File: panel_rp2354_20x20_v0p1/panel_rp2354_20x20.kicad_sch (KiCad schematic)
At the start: 0 parts

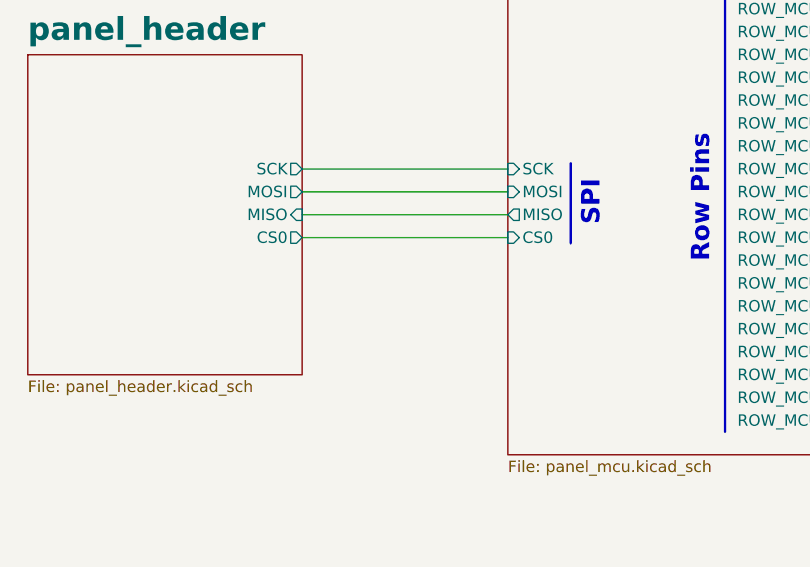
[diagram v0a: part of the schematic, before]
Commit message: Add MISO series resistor and connect EINT to MCU
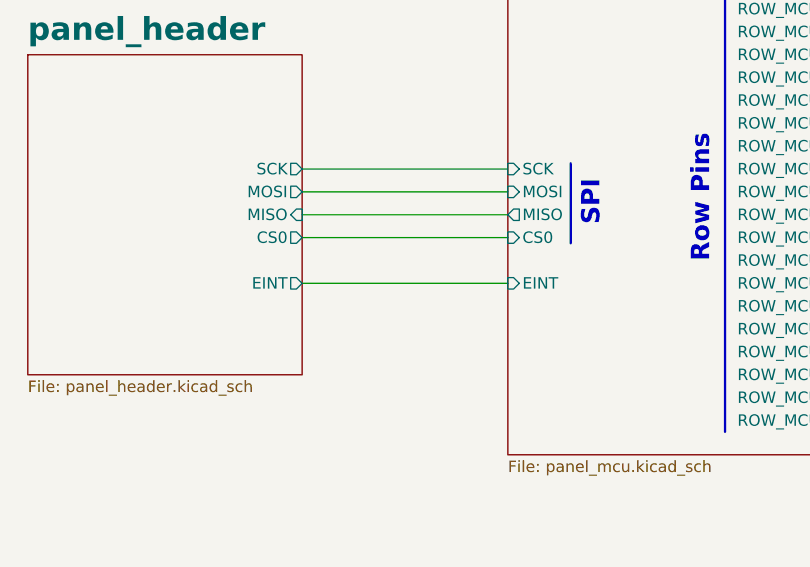
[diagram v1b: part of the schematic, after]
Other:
- sheet panel_header ports: added EINT; removed none
- sheet panel_mcu ports: added EINT; removed none
- company: (none) -> Janelia Research Campus
- title: (none) -> G6 Panel
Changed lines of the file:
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@@
 	(paper "USLetter")
 	(title_block
-		(date "9 may 2016")
+		(title "G6 Panel")
+		(date "2026-04-02")
+		(rev "0.2.0")
+		(company "Janelia Research Campus")
 	)
 	(text "Column Pins"
@@
 	(wire
 		(pts
+			(xy 60.96 132.08) (xy 83.82 132.08)
+		)
+		(stroke
+			(width 0)
+			(type default)
+		)
+	)
+	(wire
+		(pts
 			(xy 123.19 83.82) (xy 146.05 83.82)
 		)
@@
 			)
 		)
+		(pin "EINT" output
+			(at 60.96 132.08 0)
+			(effects
+				(font
+					(size 1.27 1.27)
+				)
+				(justify right)
+			)
+		)
 		(instances
 			(project "panel_rp2354_20x20"
@@
 			)
 		)
+		(pin "EINT" input
+			(at 83.82 132.08 180)
+			(effects
+				(font
+					(size 1.27 1.27)
+				)
+				(justify left)
+			)
+		)
